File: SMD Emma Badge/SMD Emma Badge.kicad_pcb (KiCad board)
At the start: 2 copper layers, 87.6 x 63.5 mm, 179 parts, among them J101 Conn_01x02_Male, Q501 MMBT3904, Q601 MMBT3904, Q701 MMBT3904, Q801 MMBT3904, U101 AMS1117-5.0, U201 LM555xM, U301 LM555xM, U401 74164, U402 74LS595, U403 74164, U404 74HC04, U405 74HC86

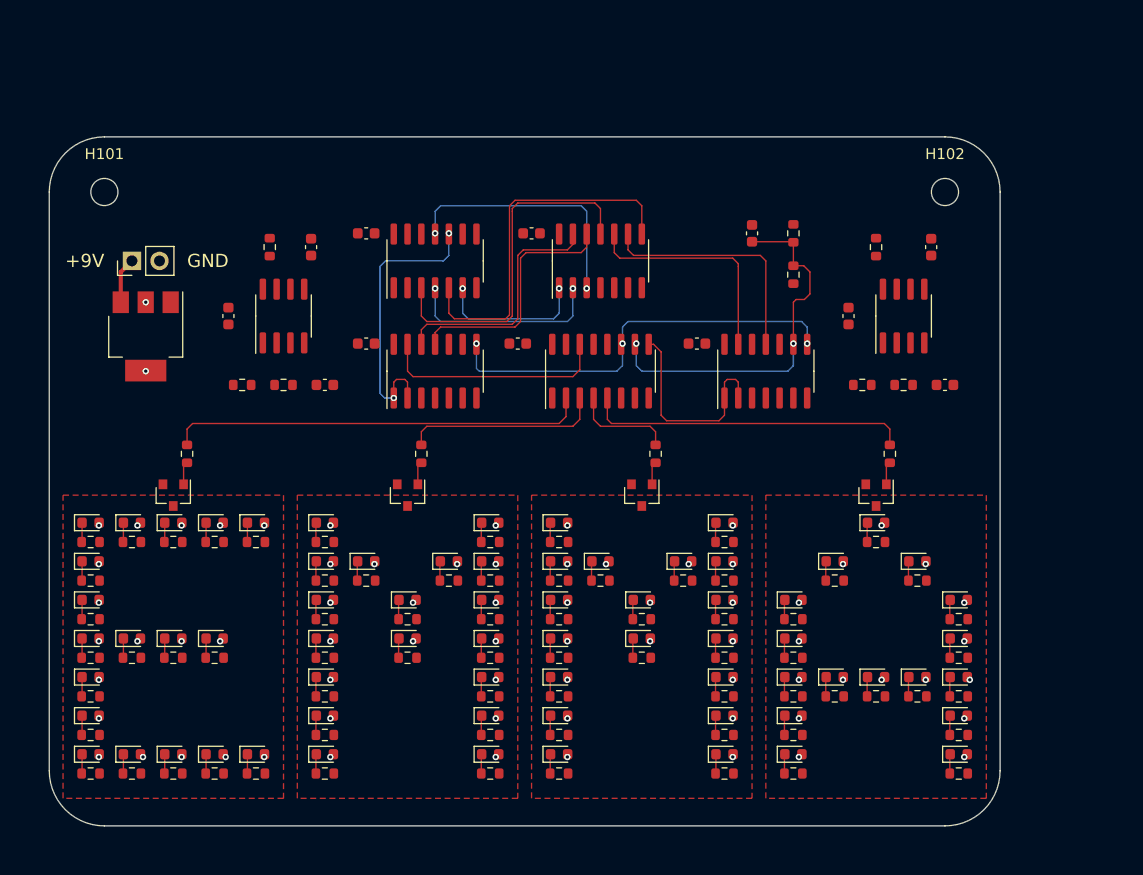
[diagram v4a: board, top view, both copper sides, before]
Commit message: Fix output enable, and do some routing
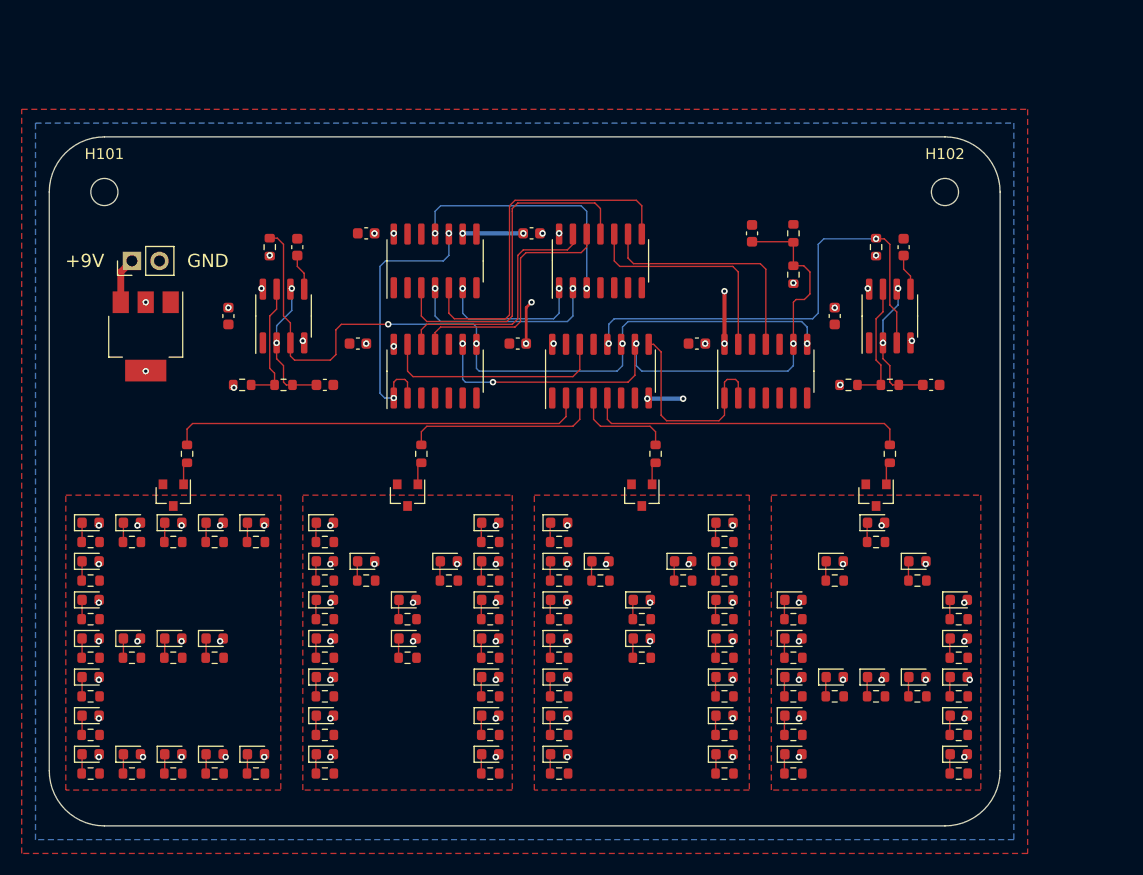
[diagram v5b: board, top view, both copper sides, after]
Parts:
- moved C203 2.54 mm to (144.8, 82.5)
- moved C202 1.27 mm to (147.3, 95.2)
- moved R202 1.27 mm to (139.7, 95.2)
- moved R203 1.27 mm to (143.5, 95.2)
- moved U201 1.27 mm to (143.5, 88.9)
- moved C303 1.27 mm to (88.9, 82.5)
- moved C201 1.27 mm to (138.4, 88.9)
- moved C403 0.76 mm to (94.5, 91.4)
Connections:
- U402 pad 13: +5V -> GND
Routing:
- net /Display Clock/CLK: track 0.00 -> 44.2 mm, vias 0 -> 2
- net /Register Clock/CLK: track 38.6 -> 72.3 mm, vias 3 -> 4
- net /LFSR/PWRCLR: track 34.5 -> 56.9 mm, vias 2 -> 4
- net Net-(C302-Pad1): track 0.00 -> 12.6 mm, vias 0 -> 2
- net Net-(C202-Pad1): track 0.00 -> 12.6 mm, vias 0 -> 2
- net Net-(R302-Pad2): track 0.00 -> 11.4 mm
- net Net-(R202-Pad2): track 0.00 -> 11.4 mm
- net +5V: track 0.00 -> 8.91 mm, vias 72 -> 95
- net GND: track 0.00 -> 8.89 mm, vias 0 -> 4
- net Net-(C303-Pad1): track 0.00 -> 3.36 mm
- net Net-(C203-Pad1): track 0.00 -> 3.36 mm
- added copper zone on B.Cu, net +5V
- added copper zone on F.Cu, net GND
